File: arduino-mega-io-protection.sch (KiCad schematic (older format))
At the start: 32 parts, among them J101 CONN_01X02, J102 CONN_01X02, J103 CONN_01X02, J104 CONN_01X02, J105 CONN_01X02, J106 CONN_01X02, J107 CONN_01X02, J108 CONN_01X36, J109 CONN_01X10, J110 CONN_02X18, J111 CONN_01X08, J112 CONN_01X08, J113 CONN_01X08, J114 CONN_01X08, J115 CONN_01X08, J116 CONN_01X02, J117 CONN_01X02, J118 CONN_01X02

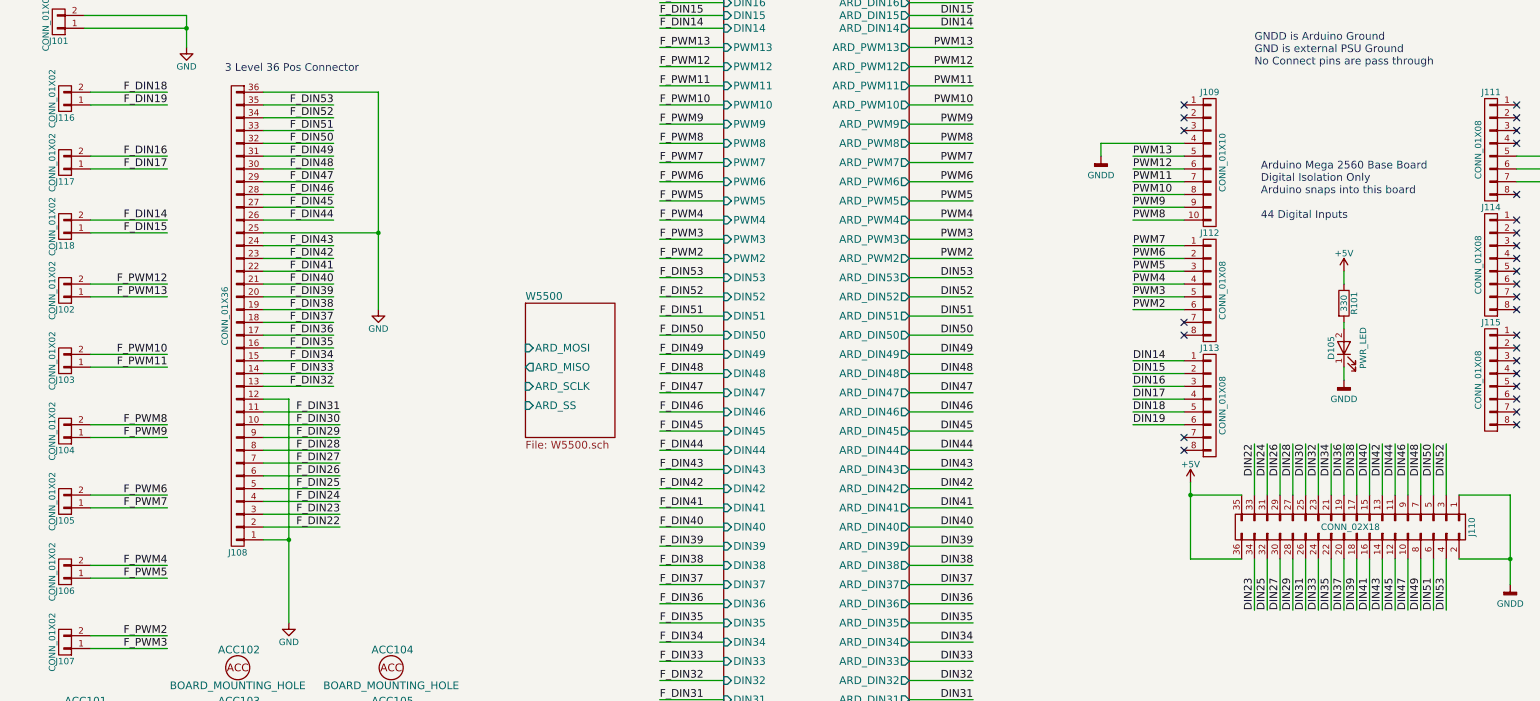
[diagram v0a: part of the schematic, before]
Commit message: connecting spi lines and cleaning-up I/O
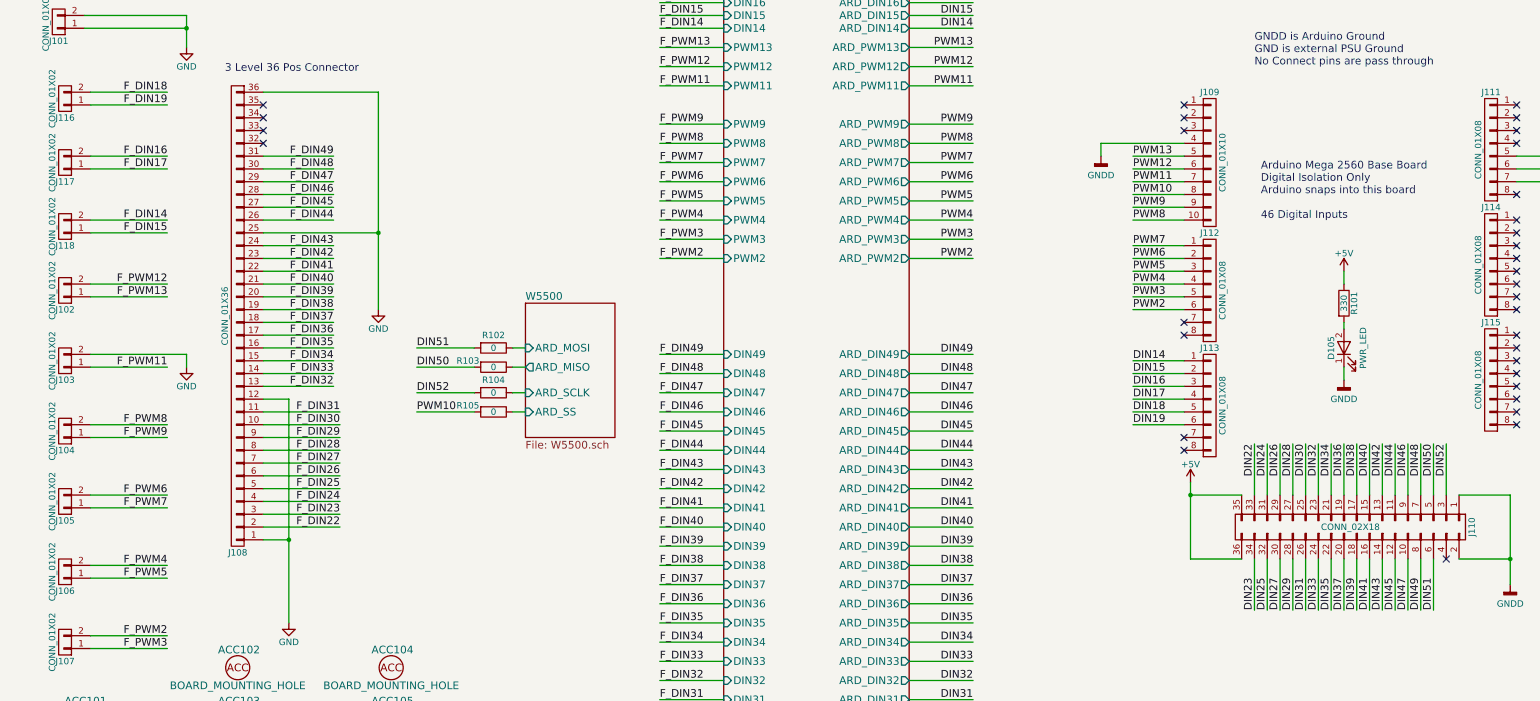
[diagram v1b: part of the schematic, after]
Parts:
- added R102, R103, R104, R105: 0, Resistors_SMD:R_0805, symbol R
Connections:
- net F_PWM10 is gone; now on net GND: J103.2 (P2)
- net DIN50: now also R103.2
- net DIN51: now also R102.2
- net DIN52: now also R104.2
- net PWM10: now also R105.2
- net W5500/ARD_MISO: now also R103.1
- net W5500/ARD_MOSI: now also R102.1
- net W5500/ARD_SCLK: now also R104.1
- net W5500/ARD_SS: now also R105.1
- net DIN53: no longer names the net of J110.4 (P4)
- net F_DIN50: no longer names the net of J108.32 (P32)
- net F_DIN51: no longer names the net of J108.33 (P33)
- net F_DIN52: no longer names the net of J108.34 (P34)
- net F_DIN53: no longer names the net of J108.35 (P35)
- no-connect marks 28 -> 33
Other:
- note added: "Arduino Mega 2560 Base Board\nDigital Isolation Only\nArduino snaps into this board\n\n46 Digital Inputs"
- note removed: "Arduino Mega 2560 Base Board\nDigital Isolation Only\nArduino snaps into this board\n\n44 Digital Inputs"

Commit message: more tweaks
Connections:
- net +5V: no longer J111.5 (P5)
- net +3V3: now reaches J111.4 (P4)
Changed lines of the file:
@@
 Arduino Mega 2560 Base Board\nDigital Isolation Only\nArduino snaps into this board\n\n46 Digital Inputs
-$Comp
-L +5V #PWR109
-U 1 1 58FCCC40
-P 13000 2050
-F 0 "#PWR109" H 13000 1900 50  0001 C CNN
-F 1 "+5V" H 13000 2190 50  0000 C CNN
-F 2 "" H 13000 2050 50  0001 C CNN
-F 3 "" H 13000 2050 50  0001 C CNN
-	1    13000 2050
-	1    0    0    -1
-$EndComp
 $Comp
 L +5V #PWR105
@@
 Wire Wire Line
 	11600 5750 11600 5350
-Wire Wire Line
-	12250 2200 13000 2200
-Wire Wire Line
-	13000 2200 13000 2050
 Wire Wire Line
 	9700 4850 10100 4850
@@
 NoConn ~ 12250 1900
 NoConn ~ 12250 2000
-NoConn ~ 12250 2100
 NoConn ~ 12250 2500
 $Comp
@@
 F91 "ARD_DIN19" O R 7500 700 60
 $EndSheet
+Wire Wire Line
+	12250 2100 12800 2100
+Wire Wire Line
+	12800 2100 12800 1950
+$Comp
+L +3V3 #PWR?
+U 1 1 593B9628
+P 12800 1950
+F 0 "#PWR?" H 12800 1800 50  0001 C CNN
+F 1 "+3V3" H 12800 2090 50  0000 C CNN
+F 2 "" H 12800 1950 50  0001 C CNN
+F 3 "" H 12800 1950 50  0001 C CNN
+	1    12800 1950
+	1    0    0    -1
+$EndComp
+NoConn ~ 12250 2200
 $EndSCHEMATC

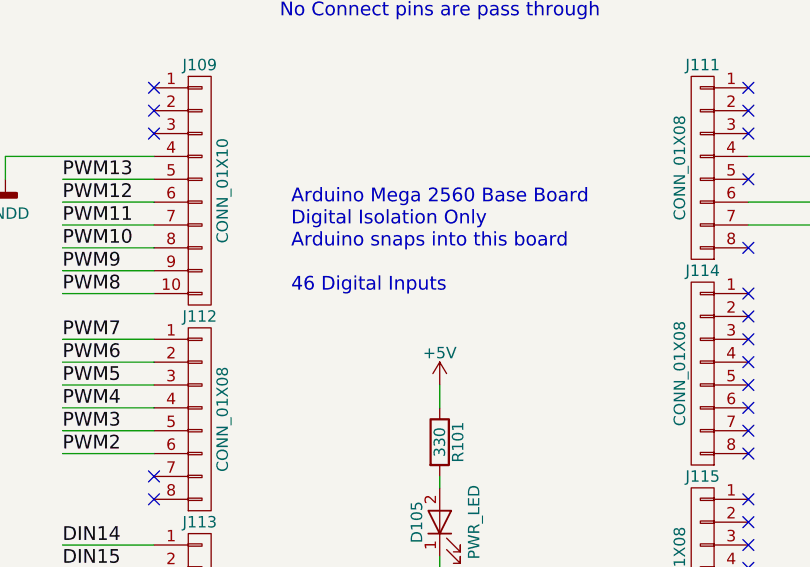
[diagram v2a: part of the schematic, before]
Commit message: almost final design - just need to add protection diodes
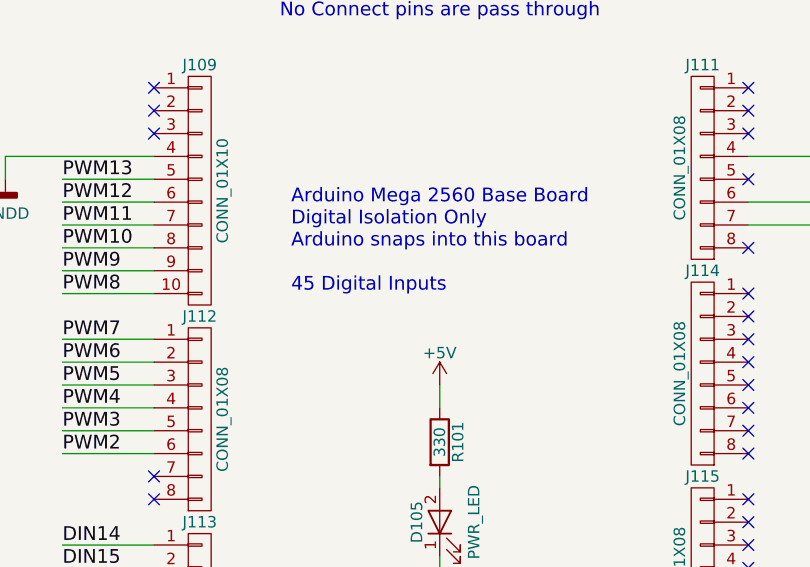
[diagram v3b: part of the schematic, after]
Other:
- note added: "Arduino Mega 2560 Base Board\nDigital Isolation Only\nArduino snaps into this board\n\n45 Digital Inputs"
- note removed: "Arduino Mega 2560 Base Board\nDigital Isolation Only\nArduino snaps into this board\n\n46 Digital Inputs"
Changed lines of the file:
@@
 $EndComp
 $Comp
-L GNDD #PWR110
+L GNDD #PWR01
 U 1 1 58FCB2DA
 P 13000 2400
-F 0 "#PWR110" H 13000 2150 50  0001 C CNN
+F 0 "#PWR01" H 13000 2150 50  0001 C CNN
 F 1 "GNDD" H 13000 2250 50  0000 C CNN
 F 2 "" H 13000 2400 50  0001 C CNN
@@
 GNDD is Arduino Ground\nGND is external PSU Ground\nNo Connect pins are pass through
 $Comp
-L GNDD #PWR104
+L GNDD #PWR02
 U 1 1 58FCB7A0
 P 9000 2200
-F 0 "#PWR104" H 9000 1950 50  0001 C CNN
+F 0 "#PWR02" H 9000 1950 50  0001 C CNN
 F 1 "GNDD" H 9000 2050 50  0000 C CNN
 F 2 "" H 9000 2200 50  0001 C CNN
@@
 PWM2
 $Comp
-L GNDD #PWR108
+L GNDD #PWR03
 U 1 1 58FCBB63
 P 12200 5550
-F 0 "#PWR108" H 12200 5300 50  0001 C CNN
+F 0 "#PWR03" H 12200 5300 50  0001 C CNN
 F 1 "GNDD" H 12200 5400 50  0000 C CNN
 F 2 "" H 12200 5550 50  0001 C CNN
@@
 DIN23
 Text Notes 10250 2700 0    60   ~ 0
-Arduino Mega 2560 Base Board\nDigital Isolation Only\nArduino snaps into this board\n\n46 Digital Inputs
-$Comp
-L +5V #PWR105
+Arduino Mega 2560 Base Board\nDigital Isolation Only\nArduino snaps into this board\n\n45 Digital Inputs
+$Comp
+L +5V #PWR04
 U 1 1 58FCCFA3
 P 9700 4750
-F 0 "#PWR105" H 9700 4600 50  0001 C CNN
+F 0 "#PWR04" H 9700 4600 50  0001 C CNN
 F 1 "+5V" H 9700 4890 50  0000 C CNN
 F 2 "" H 9700 4750 50  0001 C CNN
@@
 $EndComp
 $Comp
-L +5V #PWR106
+L +5V #PWR05
 U 1 1 58FD2DC5
 P 10900 3100
-F 0 "#PWR106" H 10900 2950 50  0001 C CNN
+F 0 "#PWR05" H 10900 2950 50  0001 C CNN
 F 1 "+5V" H 10900 3240 50  0000 C CNN
 F 2 "" H 10900 3100 50  0001 C CNN
@@
 $EndComp
 $Comp
-L GNDD #PWR107
+L GNDD #PWR06
 U 1 1 58FD2EBC
 P 10900 3950
-F 0 "#PWR107" H 10900 3700 50  0001 C CNN
+F 0 "#PWR06" H 10900 3700 50  0001 C CNN
 F 1 "GNDD" H 10900 3800 50  0000 C CNN
 F 2 "" H 10900 3950 50  0001 C CNN
@@
 $EndComp
 $Comp
-L GND #PWR103
+L GND #PWR07
 U 1 1 59059872
 P 3350 3400
-F 0 "#PWR103" H 3350 3150 50  0001 C CNN
+F 0 "#PWR07" H 3350 3150 50  0001 C CNN
 F 1 "GND" H 3350 3250 50  0000 C CNN
 F 2 "" H 3350 3400 50  0001 C CNN
@@
 $EndComp
 $Comp
-L GND #PWR102
+L GND #PWR08
 U 1 1 59059ABB
 P 2650 5850
-F 0 "#PWR102" H 2650 5600 50  0001 C CNN
+F 0 "#PWR08" H 2650 5600 50  0001 C CNN
 F 1 "GND" H 2650 5700 50  0000 C CNN
 F 2 "" H 2650 5850 50  0001 C CNN
@@
 Connection ~ 1850 1200
 $Comp
-L GND #PWR101
+L GND #PWR09
 U 1 1 59009141
 P 1850 1350
-F 0 "#PWR101" H 1850 1100 50  0001 C CNN
+F 0 "#PWR09" H 1850 1100 50  0001 C CNN
 F 1 "GND" H 1850 1200 50  0000 C CNN
 F 2 "" H 1850 1350 50  0001 C CNN
@@
 	1850 3750 1850 3850
 $Comp
-L GND #PWR?
+L GND #PWR010
 U 1 1 593C6552
 P 1850 3850
-F 0 "#PWR?" H 1850 3600 50  0001 C CNN
+F 0 "#PWR010" H 1850 3600 50  0001 C CNN
 F 1 "GND" H 1850 3700 50  0000 C CNN
 F 2 "" H 1850 3850 50  0001 C CNN
@@
 	12800 2100 12800 1950
 $Comp
-L +3V3 #PWR?
+L +3V3 #PWR011
 U 1 1 593B9628
 P 12800 1950
-F 0 "#PWR?" H 12800 1800 50  0001 C CNN
+F 0 "#PWR011" H 12800 1800 50  0001 C CNN
 F 1 "+3V3" H 12800 2090 50  0000 C CNN
 F 2 "" H 12800 1950 50  0001 C CNN

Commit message: fixing BOM for arduino connectors and updating some other items
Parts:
- J109: Characteristics Value -> X; Description Value -> X; MFN Sullins Connector Solutions -> X; MPN PRPC010SAAN-RC -> X; Package ID Value -> X
- J111, J113, J114, J115: Characteristics Value -> X; Description Value -> X; MFN Value -> X; MPN Value -> X; Package ID Value -> X; Populate (none) -> 1
- J112: Characteristics Value -> X; Description Value -> X; MFN Sullins Connector Solutions -> X; MPN PRPC008SAAN-RC -> X; Package ID Value -> X
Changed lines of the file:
@@
 LIBS:3ML_LLC_Component_Library
 LIBS:arduino_shieldsNCL
-LIBS:3ML_RJ45
-LIBS:3ML_W5500
 LIBS:switches
 LIBS:arduino-mega-io-protection-cache
@@
 F 1 "CONN_01X10" V 9950 2250 50  0000 C CNN
 F 2 "Pin_Headers:Pin_Header_Straight_1x10_Pitch2.54mm" H 9850 2250 50  0001 C CNN
-F 3 "" H 9850 2250 50  0001 C CNN
-F 4 "Value" H 9850 2250 60  0001 C CNN "Characteristics"
-F 5 "Value" H 9850 2250 60  0001 C CNN "Description"
-F 6 "Sullins Connector Solutions" H 9850 2250 60  0001 C CNN "MFN"
-F 7 "Value" H 9850 2250 60  0001 C CNN "Package ID"
+F 3 "X" H 9850 2250 50  0001 C CNN
+F 4 "X" H 9850 2250 60  0001 C CNN "Characteristics"
+F 5 "X" H 9850 2250 60  0001 C CNN "Description"
+F 6 "X" H 9850 2250 60  0001 C CNN "MFN"
+F 7 "X" H 9850 2250 60  0001 C CNN "Package ID"
 F 8 "Digikey" H 9850 2250 60  0001 C CNN "Source"
 F 9 "Y" H 9850 2250 60  0001 C CNN "Critical"
 F 10 "X" H 9850 2250 60  0001 C CNN "Notes"
 F 11 "1" H 9850 2250 60  0001 C CNN "Populate"
-F 12 "PRPC010SAAN-RC" H 9850 2250 60  0001 C CNN "MPN"
+F 12 "X" H 9850 2250 60  0001 C CNN "MPN"
 	1    9850 2250
 	1    0    0    -1
@@
 F 1 "CONN_01X08" V 9950 3250 50  0000 C CNN
 F 2 "Pin_Headers:Pin_Header_Straight_1x08_Pitch2.54mm" H 9850 3250 50  0001 C CNN
-F 3 "" H 9850 3250 50  0001 C CNN
-F 4 "Value" H 9850 3250 60  0001 C CNN "Characteristics"
-F 5 "Value" H 9850 3250 60  0001 C CNN "Description"
-F 6 "Sullins Connector Solutions" H 9850 3250 60  0001 C CNN "MFN"
-F 7 "Value" H 9850 3250 60  0001 C CNN "Package ID"
+F 3 "X" H 9850 3250 50  0001 C CNN
+F 4 "X" H 9850 3250 60  0001 C CNN "Characteristics"
+F 5 "X" H 9850 3250 60  0001 C CNN "Description"
+F 6 "X" H 9850 3250 60  0001 C CNN "MFN"
+F 7 "X" H 9850 3250 60  0001 C CNN "Package ID"
 F 8 "Digikey" H 9850 3250 60  0001 C CNN "Source"
 F 9 "Y" H 9850 3250 60  0001 C CNN "Critical"
 F 10 "X" H 9850 3250 60  0001 C CNN "Notes"
 F 11 "1" H 9850 3250 60  0001 C CNN "Populate"
-F 12 "PRPC008SAAN-RC" H 9850 3250 60  0001 C CNN "MPN"
+F 12 "X" H 9850 3250 60  0001 C CNN "MPN"
 	1    9850 3250
 	1    0    0    -1
@@
 F 1 "CONN_01X08" V 9950 4150 50  0000 C CNN
 F 2 "Pin_Headers:Pin_Header_Straight_1x08_Pitch2.54mm" H 9850 4150 50  0001 C CNN
-F 3 "" H 9850 4150 50  0001 C CNN
-F 4 "Value" H 9850 4150 60  0001 C CNN "MPN"
-F 5 "Value" H 9850 4150 60  0001 C CNN "MFN"
-F 6 "Value" H 9850 4150 60  0001 C CNN "Characteristics"
-F 7 "Value" H 9850 4150 60  0001 C CNN "Description"
-F 8 "Value" H 9850 4150 60  0001 C CNN "Package ID"
-F 9 "Digikey" H 9850 4150 60  0001 C CNN "Source"
-F 10 "Y" H 9850 4150 60  0001 C CNN "Critical"
-F 11 "X" H 9850 4150 60  0001 C CNN "Notes"
+F 3 "X" H 9850 4150 50  0001 C CNN
+F 4 "X" H 9850 4150 60  0001 C CNN "Characteristics"
+F 5 "X" H 9850 4150 60  0001 C CNN "Description"
+F 6 "X" H 9850 4150 60  0001 C CNN "MFN"
+F 7 "X" H 9850 4150 60  0001 C CNN "Package ID"
+F 8 "Digikey" H 9850 4150 60  0001 C CNN "Source"
+F 9 "Y" H 9850 4150 60  0001 C CNN "Critical"
+F 10 "X" H 9850 4150 60  0001 C CNN "Notes"
+F 11 "1" H 9850 4150 60  0001 C CNN "Populate"
+F 12 "X" H 9850 4150 60  0001 C CNN "MPN"
 	1    9850 4150
 	1    0    0    -1
@@
 F 1 "CONN_01X08" V 12150 2150 50  0000 C CNN
 F 2 "Pin_Headers:Pin_Header_Straight_1x08_Pitch2.54mm" H 12050 2150 50  0001 C CNN
-F 3 "" H 12050 2150 50  0001 C CNN
-F 4 "Value" H 12050 2150 60  0001 C CNN "MPN"
-F 5 "Value" H 12050 2150 60  0001 C CNN "MFN"
-F 6 "Value" H 12050 2150 60  0001 C CNN "Characteristics"
-F 7 "Value" H 12050 2150 60  0001 C CNN "Description"
-F 8 "Value" H 12050 2150 60  0001 C CNN "Package ID"
-F 9 "Digikey" H 12050 2150 60  0001 C CNN "Source"
-F 10 "Y" H 12050 2150 60  0001 C CNN "Critical"
-F 11 "X" H 12050 2150 60  0001 C CNN "Notes"
+F 3 "X" H 12050 2150 50  0001 C CNN
+F 4 "X" H 12050 2150 60  0001 C CNN "Characteristics"
+F 5 "X" H 12050 2150 60  0001 C CNN "Description"
+F 6 "X" H 12050 2150 60  0001 C CNN "MFN"
+F 7 "X" H 12050 2150 60  0001 C CNN "Package ID"
+F 8 "Digikey" H 12050 2150 60  0001 C CNN "Source"
+F 9 "Y" H 12050 2150 60  0001 C CNN "Critical"
+F 10 "X" H 12050 2150 60  0001 C CNN "Notes"
+F 11 "1" H 12050 2150 60  0001 C CNN "Populate"
+F 12 "X" H 12050 2150 60  0001 C CNN "MPN"
 	1    12050 2150
 	-1   0    0    -1
@@
 F 1 "CONN_01X08" V 12150 3050 50  0000 C CNN
 F 2 "Pin_Headers:Pin_Header_Straight_1x08_Pitch2.54mm" H 12050 3050 50  0001 C CNN
-F 3 "" H 12050 3050 50  0001 C CNN
-F 4 "Value" H 12050 3050 60  0001 C CNN "MPN"
-F 5 "Value" H 12050 3050 60  0001 C CNN "MFN"
-F 6 "Value" H 12050 3050 60  0001 C CNN "Characteristics"
-F 7 "Value" H 12050 3050 60  0001 C CNN "Description"
-F 8 "Value" H 12050 3050 60  0001 C CNN "Package ID"
-F 9 "Digikey" H 12050 3050 60  0001 C CNN "Source"
-F 10 "Y" H 12050 3050 60  0001 C CNN "Critical"
-F 11 "X" H 12050 3050 60  0001 C CNN "Notes"
+F 3 "X" H 12050 3050 50  0001 C CNN
+F 4 "X" H 12050 3050 60  0001 C CNN "Characteristics"
+F 5 "X" H 12050 3050 60  0001 C CNN "Description"
+F 6 "X" H 12050 3050 60  0001 C CNN "MFN"
+F 7 "X" H 12050 3050 60  0001 C CNN "Package ID"
+F 8 "Digikey" H 12050 3050 60  0001 C CNN "Source"
+F 9 "Y" H 12050 3050 60  0001 C CNN "Critical"
+F 10 "X" H 12050 3050 60  0001 C CNN "Notes"
+F 11 "1" H 12050 3050 60  0001 C CNN "Populate"
+F 12 "X" H 12050 3050 60  0001 C CNN "MPN"
 	1    12050 3050
 	-1   0    0    -1
@@
 F 1 "CONN_01X08" V 12150 3950 50  0000 C CNN
 F 2 "Pin_Headers:Pin_Header_Straight_1x08_Pitch2.54mm" H 12050 3950 50  0001 C CNN
-F 3 "" H 12050 3950 50  0001 C CNN
-F 4 "Value" H 12050 3950 60  0001 C CNN "MPN"
-F 5 "Value" H 12050 3950 60  0001 C CNN "MFN"
-F 6 "Value" H 12050 3950 60  0001 C CNN "Characteristics"
-F 7 "Value" H 12050 3950 60  0001 C CNN "Description"
-F 8 "Value" H 12050 3950 60  0001 C CNN "Package ID"
-F 9 "Digikey" H 12050 3950 60  0001 C CNN "Source"
-F 10 "Y" H 12050 3950 60  0001 C CNN "Critical"
-F 11 "X" H 12050 3950 60  0001 C CNN "Notes"
+F 3 "X" H 12050 3950 50  0001 C CNN
+F 4 "X" H 12050 3950 60  0001 C CNN "Characteristics"
+F 5 "X" H 12050 3950 60  0001 C CNN "Description"
+F 6 "X" H 12050 3950 60  0001 C CNN "MFN"
+F 7 "X" H 12050 3950 60  0001 C CNN "Package ID"
+F 8 "Digikey" H 12050 3950 60  0001 C CNN "Source"
+F 9 "Y" H 12050 3950 60  0001 C CNN "Critical"
+F 10 "X" H 12050 3950 60  0001 C CNN "Notes"
+F 11 "1" H 12050 3950 60  0001 C CNN "Populate"
+F 12 "X" H 12050 3950 60  0001 C CNN "MPN"
 	1    12050 3950
 	-1   0    0    -1
